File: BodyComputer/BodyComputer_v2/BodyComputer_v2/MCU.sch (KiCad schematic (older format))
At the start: 49 parts

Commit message: Second version of the body computer - WIP
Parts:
- removed R?: 0R, Resistor_SMD:R_0402_1005Metric, symbol Device:R_Small
- removed R? (x6): 10k, Resistor_SMD:R_0402_1005Metric, symbol Device:R_Small
- removed R?: 1k5, Resistor_SMD:R_0402_1005Metric, symbol Device:R_Small
- removed R? (x4): 47k, Resistor_SMD:R_0402_1005Metric, symbol Device:R_Small
- removed TP?: TestPoint, TestPoint:TestPoint_Pad_1.0x1.0mm, symbol Connector:TestPoint_Flag
- removed U?: STM32F429ZGTx, Package_QFP:LQFP-144_20x20mm_P0.5mm, symbol MCU_ST_STM32F4:STM32F429ZGTx
- added C? (x3): 100n, Capacitor_SMD:C_0402_1005Metric, symbol Device:C_Small
- added J?: Conn_02x07_Odd_Even, Connector_PinHeader_1.27mm:PinHeader_2x07_P1.27mm_Vertical_SMD, symbol Connector_Generic:Conn_02x07_Odd_Even
- added J?: Conn_01x03, Connector_PinHeader_2.54mm:PinHeader_1x03_P2.54mm_Vertical, symbol Connector_Generic:Conn_01x03
- added R?: NULL, Resistor_SMD:R_0402_1005Metric, symbol Device:R_Small
- added R?: 10k, Resistor_SMD:R_0402_1005Metric, symbol Device:R_Small
- added U?: STM32F407IGTx, Package_QFP:LQFP-176_24x24mm_P0.5mm, symbol MCU_ST_STM32F4:STM32F407IGTx
- Y?: footprint (none) -> Crystal:Crystal_C38-LF_D3.0mm_L8.0mm_Vertical
- Y?: footprint (none) -> Crystal:Crystal_HC49-4H_Vertical
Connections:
- net labels added: ADC_0, ADC_1, ADC_10, ADC_11, ADC_12, ADC_13, ADC_14, ADC_15, ADC_16, ADC_17, ADC_18, ADC_19, ADC_2, ADC_20, ADC_21, ADC_22, ADC_23, ADC_3, ADC_4, ADC_5, ADC_6, ADC_7, ADC_8, ADC_9, BOOT0, BYPASS_REG, I2C2_SCL, I2C2_SDA, I2C3_SCL, I2C3_SDA, PDR_ON, SDIO_CLK, T_VCP_RX, T_VCP_TX, USART2_RX, USART2_TX, USART6_RX_NODE, USART6_TX_NODE, USB_HS_N, USB_HS_P, USB_OTG_FS_ID, USB_OTG_FS_N, USB_OTG_FS_P
- net labels removed: ADC_IN0, ADC_IN1, ADC_IN10, ADC_IN11, ADC_IN12, ADC_IN13, ADC_IN14, ADC_IN15, ADC_IN16, ADC_IN17, ADC_IN18, ADC_IN19, ADC_IN2, ADC_IN20, ADC_IN21, ADC_IN22, ADC_IN3, ADC_IN4, ADC_IN5, ADC_IN6, ADC_IN7, BUZZER_ON, EEPROM_WP1, EEPROM_WP2, ENC1_BUTTON, ENC2_BUTTON, I2C1_SCL_EEPROM, I2C1_SCL_LCD, I2C1_SDA_EEPROM, I2C1_SDA_LCD, SDIO_CK, SPI6_MISO, SPI6_MOSI, SPI6_SCK, TIM11_CH1_PWM, TIM1_CH1_ENC2_A, TIM1_CH2_ENC2_B, TIM2_CH1_PWM, TIM2_CH2_PWM, TIM2_CH4_PWM, TIM3_CH1_PWM, TIM3_CH2_PWM, TIM3_CH3_PWM, TIM3_CH4_PWM, TIM4_CH1_PWM, TIM4_CH2_PWM, TIM4_CH3_PWM, TIM4_CH4_PWM, TIM5_CH1_PWM, TIM5_CH2_PWM, TIM5_CH3_PWM, TIM5_CH4_PWM, TIM8_CH1_ENC1_A, TIM8_CH2_ENC1_B, UART7_RX_GPS, UART7_TX_GPS, USART2_RX_NODEMCU, USART2_TX_NODEMCU, USB_HS_DM, USB_HS_DP
- wire segments 332 -> 357
- no-connect marks 0 -> 4
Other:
- note added: "Debug Connector"
- moved on the sheet: C?, J?, R?

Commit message: Finished board design. Schematic names improvements needed.
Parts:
- removed R? (x2): 10k, Resistor_SMD:R_0402_1005Metric, symbol Device:R_Small
- removed R?: NULL, Resistor_SMD:R_0402_1005Metric, symbol Device:R_Small
- added C825: 100n, Capacitor_SMD:C_0402_1005Metric, symbol Device:C_Small
- added D801: LED_RED, LED_SMD:LED_0603_1608Metric, symbol Device:LED
- added D802: LED_YELLOW, LED_SMD:LED_0603_1608Metric, symbol Device:LED
- added D803: LED_GREEN, LED_SMD:LED_0603_1608Metric, symbol Device:LED
- added D804: LED_BLUE, LED_SMD:LED_0603_1608Metric, symbol Device:LED
- added J1: PinHeader, Connector_PinHeader_2.54mm:PinHeader_1x01_P2.54mm_Vertical, symbol Connector_Generic:Conn_01x01
- added J2: Conn_01x03, Connector_PinHeader_2.54mm:PinHeader_1x03_P2.54mm_Vertical, symbol Connector_Generic:Conn_01x03
- added J801: DB9_Female_MountingHoles, Connector_Dsub:DSUB-9_Female_Horizontal_P2.77x2.84mm_EdgePinOffset7.70mm_Housed_MountingHolesOffset9.12mm, symbol Connector:DB9_Female_MountingHoles
- added J802, J805: Conn_01x02, Connector_PinHeader_2.54mm:PinHeader_1x02_P2.54mm_Vertical, symbol Connector_Generic:Conn_01x02
- added Q801, Q802, Q803, Q804: NPN, Package_TO_SOT_SMD:SOT-23, symbol Device:Q_NPN_BEC
- added Q805: Q_NMOS_GSD, Package_TO_SOT_SMD:SOT-23, symbol Device:Q_NMOS_GSD
- added R801, R802, R803, R804: 470, Resistor_SMD:R_0402_1005Metric, symbol Device:R_Small
- added R805, R806, R807, R808, R810: 1k, Resistor_SMD:R_0402_1005Metric, symbol Device:R_Small
- added R809: 22, Resistor_SMD:R_0402_1005Metric, symbol Device:R_Small
- added R812: NULL, Resistor_SMD:R_0402_1005Metric, symbol Device:R_Small
- added R813, R819, R824, R825, R830: 10k, Resistor_SMD:R_0402_1005Metric, symbol Device:R_Small
- added R814, R815, R816, R817, R818: 47k, Resistor_SMD:R_0402_1005Metric, symbol Device:R_Small
- added R820, R821, R822, R823, R828, R829: 4k7, Resistor_SMD:R_0402_1005Metric, symbol Device:R_Small
- added R826, R827: 1k5, Resistor_SMD:R_0402_1005Metric, symbol Device:R_Small
- added TP807, TP808, TP809, TP810, TP813, TP814, TP816, TP817: TestPoint, Connector_PinHeader_2.54mm:PinHeader_1x01_P2.54mm_Vertical, symbol Connector:TestPoint_Flag
- L801: renamed from L?; footprint (none) -> Inductor_SMD:L_0603_1608Metric
- gave numbers to parts that had none: 39
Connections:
- net labels added: +12V, +5V, ALTERNATOR_SIGNAL, BOOT1, BRAKE_PEDAL, BUZZER, CLUTCH_PEDAL, DC_5V_ENABLE, DIAG_LED_1, DIAG_LED_1_GND_IN, DIAG_LED_2, DIAG_LED_2_GND_IN, DIAG_LED_3, DIAG_LED_3_GND_IN, DIAG_LED_4, DIAG_LED_4_GND_IN, EEPROM_WP1, EEPROM_WP2, ENCODER_1_A, ENCODER_1_B, ENCODER_1_BUTTON, ENCODER_2_A, ENCODER_2_B, ENCODER_2_BUTTON, EN_ELECTRO_CLUTCH, FAN_BOARD, FRAM_WP1, I2C1_SCL, I2C1_SDA, IN1_CNTRL_ENGINE, IN2_CNTRL_ENGINE, IN_BINARY_1, IN_BINARY_2, IN_BINARY_3, IN_BINARY_4, IN_BINARY_5, IN_BINARY_6, IN_BINARY_7, IN_BINARY_8, IN_BIN_10, IN_BIN_11, IN_BIN_12, IN_BIN_13, IN_BIN_14, IN_BIN_15, IN_BIN_16, IN_BIN_17, IN_BIN_9, IN_WIPERS_FAST, IN_WIPERS_ON, IN_WIPERS_SLOW, KEY_CRANKING, KEY_IGNITION, LED_Power, MICROSD_DETECT, MOS_P_ON_5, MOS_P_ON_6, MOS_P_ON_7, MOS_P_ON_8, OIL_PRESSURE_BIN, POWER_ON_CRUISE_CONTROL, POWER_ON_GPS, POWER_ON_LCD, POWER_ON_MICROSD, POWER_ON_NODEMCU, PWM_CRUISE_CTRL, PWM_LCD_BACKLIGHT, PWM_TIM12_1, PWM_TIM12_2, PWM_TIM4_1, PWM_TIM4_2, PWM_TIM4_3, PWM_TIM4_4, PWM_TIM5_1, PWM_TIM5_2, PWM_TIM5_3, PWM_TIM5_4, PWM_TIM8_1, PWM_TIM8_2, PWM_TIM8_4, RELAY_ON_1, RELAY_ON_2, RELAY_ON_3, RELAY_ON_4, RPM_SIGNAL, SPEED_SIGNAL, USART1_RX, USART1_TX, V_POWER, WIPERS_SIG2_ON, WIPERS_SIG3_ON, WIPERS_SIG5_ON
- wire segments 357 -> 494
- no-connect marks 4 -> 10
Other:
- note added: "Diagnostic LEDs"
- note added: "EEPROM\nI2C"
- note added: "EEPROM\nWrite\nProtection"
- note added: "FRAM\nCommunication"
- note added: "I2C LCD"
- note added: "MicroSD \nSignals"
- note added: "On - Board FAN"
- moved on the sheet: R831, R832, R835, R836

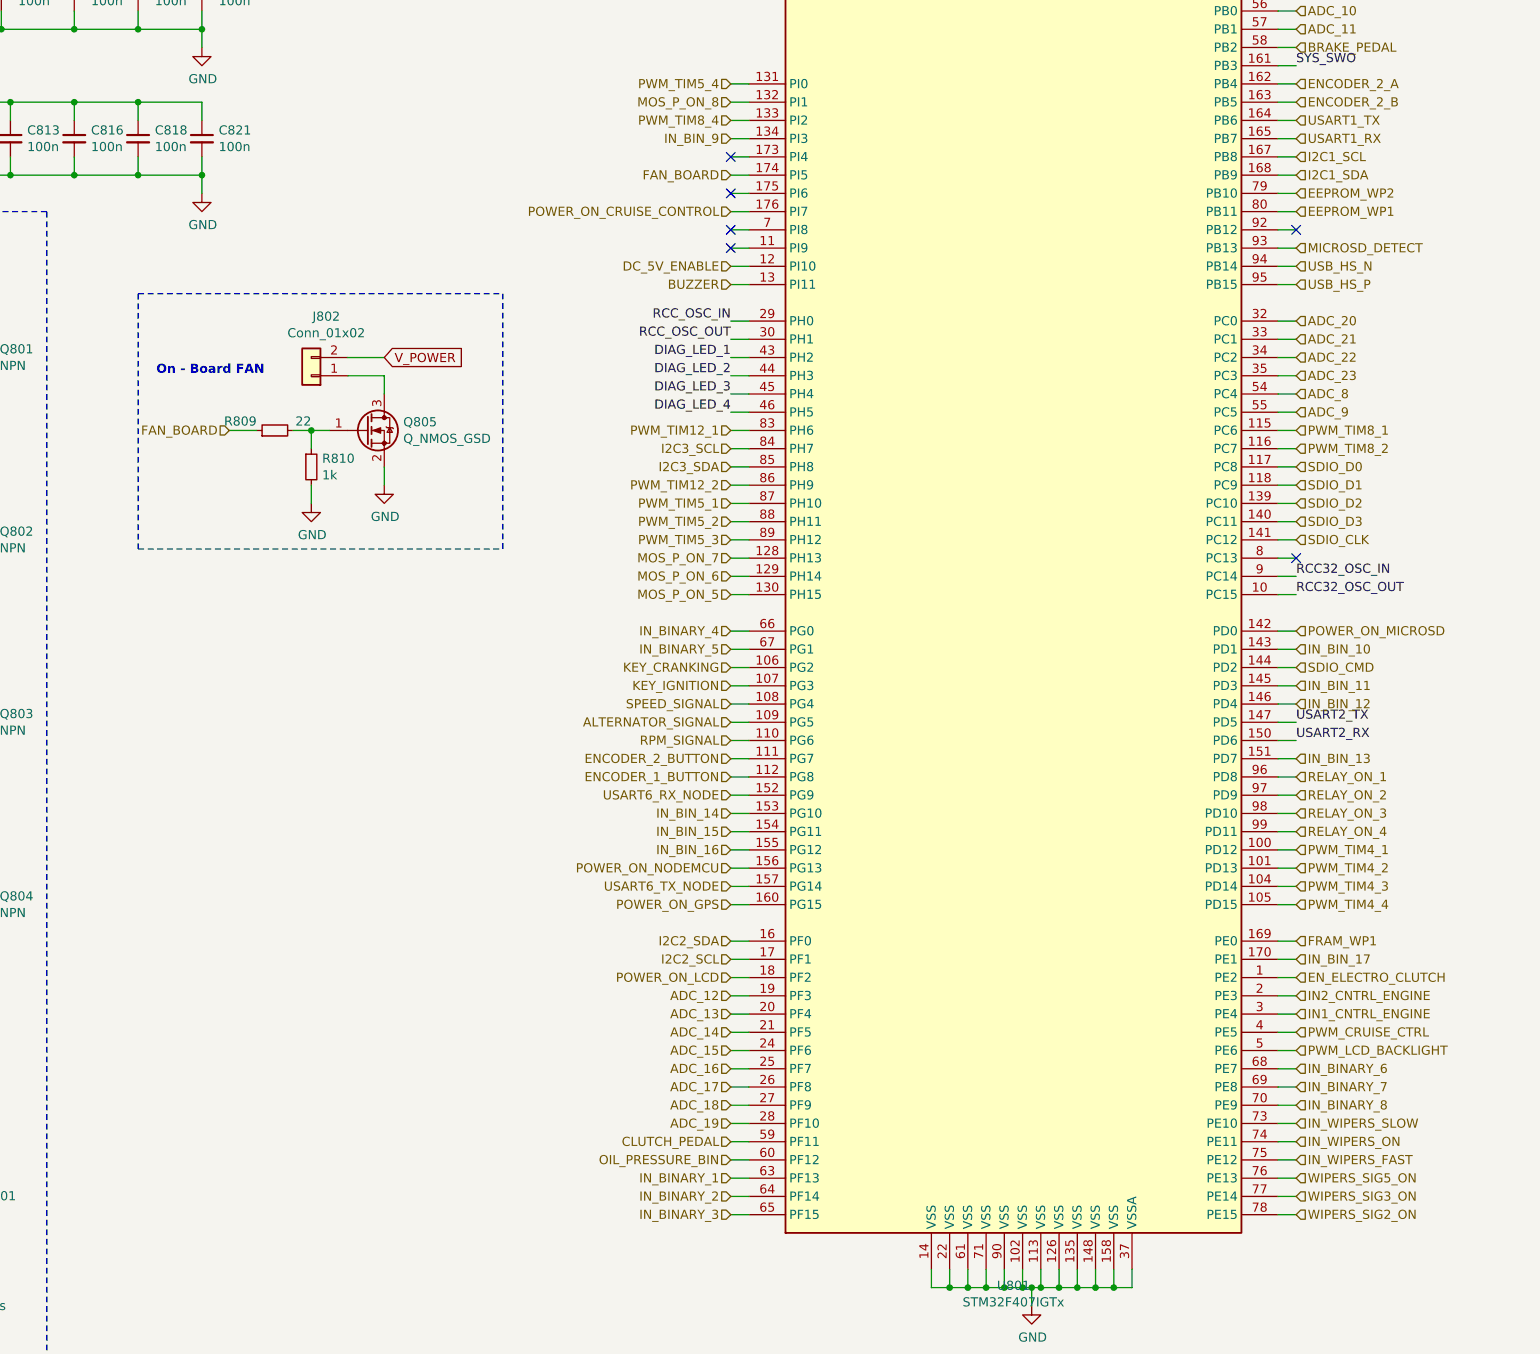
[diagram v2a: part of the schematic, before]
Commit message: Signals naming improvements
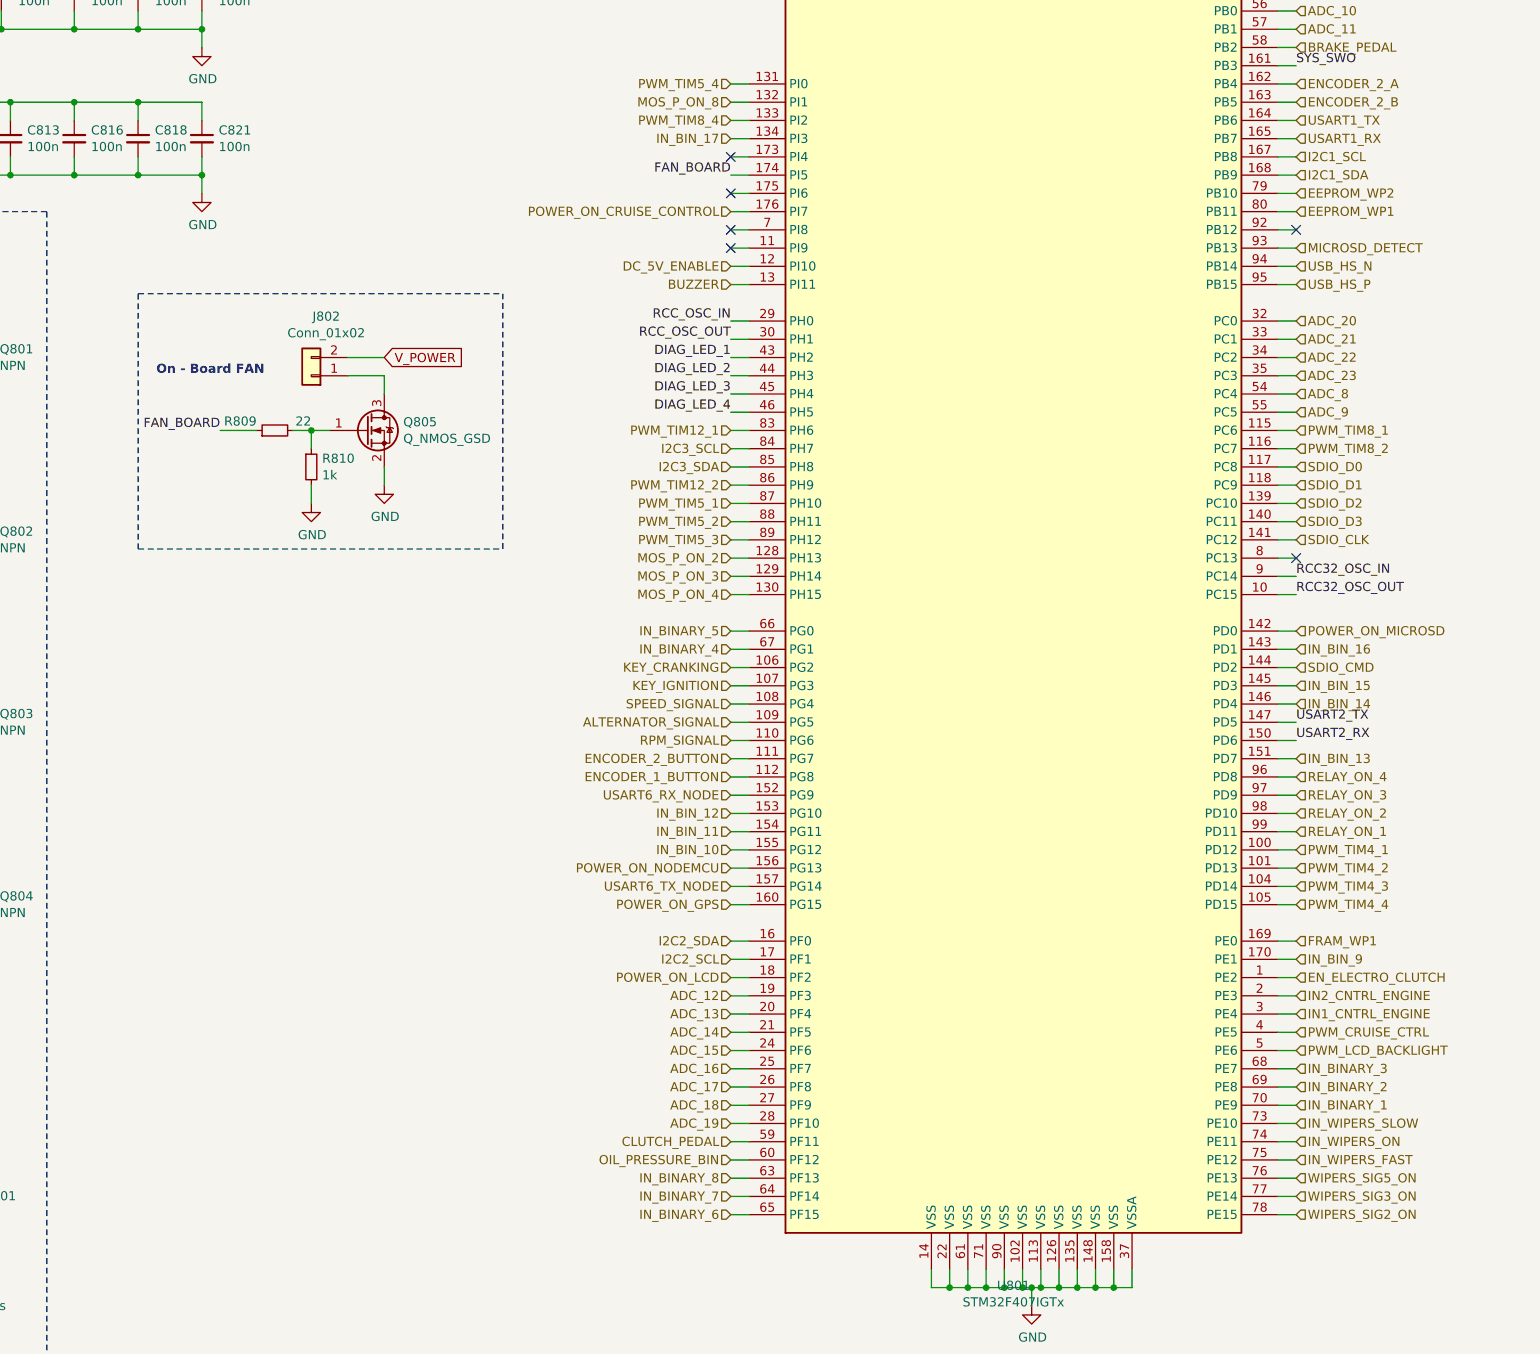
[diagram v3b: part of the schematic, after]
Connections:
- net IN_BINARY_1: now also U801.70 (PE9); no longer U801.63 (PF13)
- net IN_BINARY_2: now also U801.69 (PE8); no longer U801.64 (PF14)
- net IN_BINARY_3: now also U801.68 (PE7); no longer U801.65 (PF15)
- net IN_BINARY_4: now also U801.67 (PG1); no longer U801.66 (PG0)
- net IN_BINARY_5: now also U801.66 (PG0); no longer U801.67 (PG1)
- net IN_BINARY_6: now also U801.65 (PF15); no longer U801.68 (PE7)
- net IN_BINARY_7: now also U801.64 (PF14); no longer U801.69 (PE8)
- net IN_BINARY_8: now also U801.63 (PF13); no longer U801.70 (PE9)
- net IN_BIN_10: now also U801.155 (PG12); no longer U801.143 (PD1)
- net IN_BIN_11: now also U801.154 (PG11); no longer U801.145 (PD3)
- net IN_BIN_12: now also U801.153 (PG10); no longer U801.146 (PD4)
- net IN_BIN_14: now also U801.146 (PD4); no longer U801.153 (PG10)
- net IN_BIN_15: now also U801.145 (PD3); no longer U801.154 (PG11)
- net IN_BIN_16: now also U801.143 (PD1); no longer U801.155 (PG12)
- net IN_BIN_17: now also U801.134 (PI3); no longer U801.170 (PE1)
- net IN_BIN_9: now also U801.170 (PE1); no longer U801.134 (PI3)
- net RELAY_ON_1: now also U801.99 (PD11); no longer U801.96 (PD8)
- net RELAY_ON_2: now also U801.98 (PD10); no longer U801.97 (PD9)
- net RELAY_ON_3: now also U801.97 (PD9); no longer U801.98 (PD10)
- net RELAY_ON_4: now also U801.96 (PD8); no longer U801.99 (PD11)
- net MOS_P_ON_5 renamed MOS_P_ON_4
- net MOS_P_ON_6 renamed MOS_P_ON_3
- net MOS_P_ON_7 renamed MOS_P_ON_2
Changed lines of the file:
@@
 CLUTCH_PEDAL
 Text HLabel 6400 9900 0    50   Input ~ 0
+IN_BINARY_8
+Text HLabel 6400 10000 0    50   Input ~ 0
+IN_BINARY_7
+Text HLabel 6400 10100 0    50   Input ~ 0
+IN_BINARY_6
+Text HLabel 6400 6900 0    50   Input ~ 0
+IN_BINARY_5
+Text HLabel 6400 7000 0    50   Input ~ 0
+IN_BINARY_4
+Text HLabel 9500 9300 2    50   Input ~ 0
+IN_BINARY_3
+Text HLabel 9500 9400 2    50   Input ~ 0
+IN_BINARY_2
+Text HLabel 9500 9500 2    50   Input ~ 0
 IN_BINARY_1
-Text HLabel 6400 10000 0    50   Input ~ 0
-IN_BINARY_2
-Text HLabel 6400 10100 0    50   Input ~ 0
-IN_BINARY_3
-Text HLabel 6400 6900 0    50   Input ~ 0
-IN_BINARY_4
-Text HLabel 6400 7000 0    50   Input ~ 0
-IN_BINARY_5
-Text HLabel 9500 9300 2    50   Input ~ 0
-IN_BINARY_6
-Text HLabel 9500 9400 2    50   Input ~ 0
-IN_BINARY_7
-Text HLabel 9500 9500 2    50   Input ~ 0
-IN_BINARY_8
 Text HLabel 9500 8800 2    50   Input ~ 0
 EN_ELECTRO_CLUTCH
@@
 Text HLabel 9500 10100 2    50   Input ~ 0
 WIPERS_SIG2_ON
-Text HLabel 9500 7700 2    50   Input ~ 0
-RELAY_ON_1
 Text HLabel 9500 7800 2    50   Input ~ 0
+RELAY_ON_3
+Text HLabel 9500 7900 2    50   Input ~ 0
 RELAY_ON_2
-Text HLabel 9500 7900 2    50   Input ~ 0
-RELAY_ON_3
-Text HLabel 9500 8000 2    50   Input ~ 0
-RELAY_ON_4
 Text HLabel 6400 4900 0    50   Input ~ 0
 DC_5V_ENABLE
@@
 Connection ~ 2300 6150
 Text HLabel 6400 6700 0    50   Input ~ 0
-MOS_P_ON_5
+MOS_P_ON_4
 Text HLabel 6400 6600 0    50   Input ~ 0
-MOS_P_ON_6
+MOS_P_ON_3
 Text HLabel 6400 6500 0    50   Input ~ 0
-MOS_P_ON_7
+MOS_P_ON_2
 Text HLabel 6400 4000 0    50   Input ~ 0
 MOS_P_ON_8
 Text HLabel 6400 4200 0    50   Input ~ 0
-IN_BIN_9
+IN_BIN_17
 Text HLabel 9500 7000 2    50   Input ~ 0
-IN_BIN_10
+IN_BIN_16
 Text HLabel 9500 7200 2    50   Input ~ 0
-IN_BIN_11
+IN_BIN_15
 Text HLabel 9500 7300 2    50   Input ~ 0
-IN_BIN_12
+IN_BIN_14
 Text HLabel 9500 7600 2    50   Input ~ 0
 IN_BIN_13
 Text HLabel 6400 7900 0    50   Input ~ 0
-IN_BIN_14
+IN_BIN_12
 Text HLabel 6400 8000 0    50   Input ~ 0
-IN_BIN_15
+IN_BIN_11
 Text HLabel 6400 8100 0    50   Input ~ 0
-IN_BIN_16
+IN_BIN_10
 Text HLabel 9500 8700 2    50   Input ~ 0
-IN_BIN_17
+IN_BIN_9
 NoConn ~ 6400 4700
 NoConn ~ 6400 4800
@@
 	2150 10750 2150 10700
 Connection ~ 2150 10700
-Text HLabel 6400 4400 0    50   Input ~ 0
-FAN_BOARD
 NoConn ~ 6400 4500
 $Comp
@@
 $EndComp
 Wire Wire Line
-	3800 5800 3650 5800
-Wire Wire Line
 	4500 5600 4500 5500
-Text HLabel 3650 5800 0    50   Input ~ 0
-FAN_BOARD
 $Comp
 L Connector_Generic:Conn_01x02 J802
@@
 Text HLabel 9500 4800 2    50   Input ~ 0
 MICROSD_DETECT
+Text Label 6400 4400 2    50   ~ 0
+FAN_BOARD
+Text Label 3600 5800 2    50   ~ 0
+FAN_BOARD
+Wire Wire Line
+	3600 5800 3800 5800
+Text HLabel 9500 8000 2    50   Input ~ 0
+RELAY_ON_1
+Text HLabel 9500 7700 2    50   Input ~ 0
+RELAY_ON_4
 $EndSCHEMATC
